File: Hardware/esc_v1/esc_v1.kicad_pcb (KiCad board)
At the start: 6 copper layers, 81 x 51.1 mm, 152 parts, among them IC1 RT8259GE, J1 vcc_connector, J2 SWD_tag_connect, J3 motor_connector, J4 10118193-0001LF, Q1 IRFH7084TRPBF, Q2 IRFH7084TRPBF, Q3 IRFH7084TRPBF, Q4 IRFH7084TRPBF, Q5 IRFH7084TRPBF, Q6 IRFH7084TRPBF, SW1 SW_Push, U1 FAN7390MX, U10 MAX40056UAUA/V+, U2 AZ1117CH-3.3TRG1, U3 FAN7390MX, U4 ATSAME70J21A-AN, U5 CP2102N-Axx-xQFN24, U6 FAN7390MX, U9 MAX40056UAUA/V+, Y1 Crystal_GND2

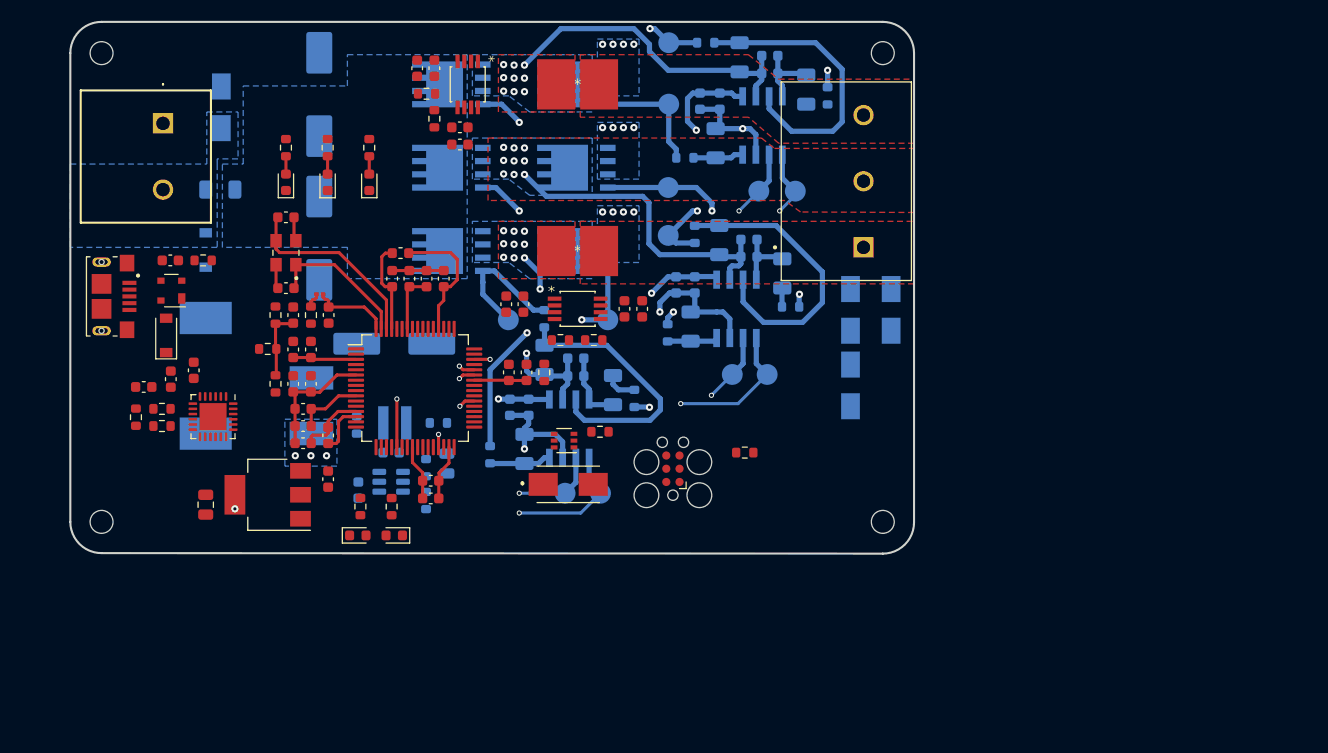
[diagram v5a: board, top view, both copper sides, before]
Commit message: Finished layout. Final check remains
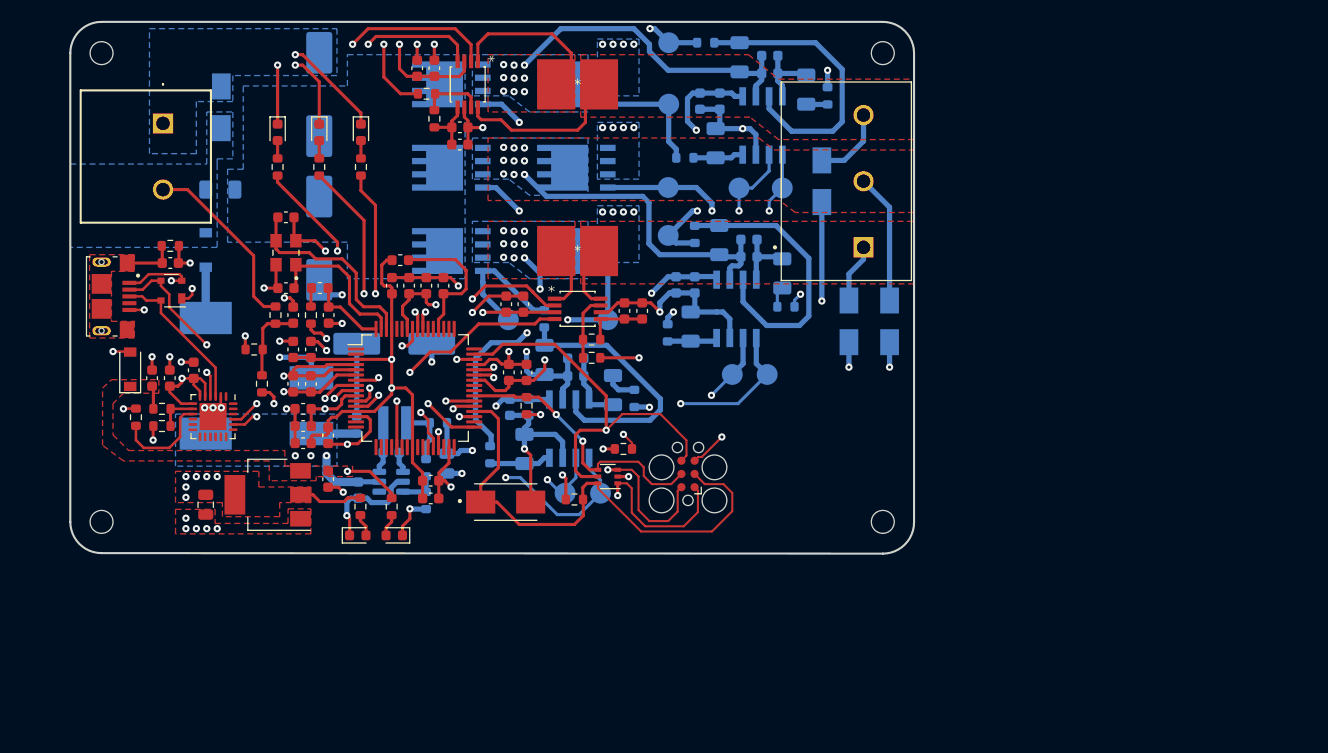
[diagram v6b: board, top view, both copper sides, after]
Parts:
- L2: footprint Inductor_SMD:L_0201_0603Metric -> Inductor_SMD:L_0603_1608Metric
- moved D8 14.0 mm to (163.6, 95.2)
- moved R14 11.7 mm to (144.5, 120.8)
- moved D1 10.0 mm to (111.3, 90.5), turned to -90 degrees
- moved R1 8.99 mm to (111.3, 93.8), turned to 90 degrees
- moved D5 8.65 mm to (119.3, 90.5), turned to -90 degrees
- moved R3 7.44 mm to (119.3, 93.8), turned to 90 degrees
- moved R16 6.95 mm to (139.8, 125.7), turned to 0 degrees
- moved SW1 6.24 mm to (132.8, 126.0)
- moved D6 6.15 mm to (166.2, 108.6)
- moved D2 5.44 mm to (143.0, 123.5)
- moved D4 4.86 mm to (115.3, 90.5), turned to -90 degrees
- moved D23 4.74 mm to (97.2, 113.2)
- moved D7 3.91 mm to (170.1, 108.6)
- moved R15 3.62 mm to (135.2, 116.7), turned to 90 degrees
- moved R33 3.45 mm to (141.4, 112.1), turned to 0 degrees
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- renumbered H0 to TP1, LO_W to TP10, HO_W to TP11, LO_W to TP12, L0 to TP2, H1 to TP3, L1 to TP4, H2 to TP5, L2 to TP6, HO_U to TP7, LO_U to TP8, HO_V to TP9
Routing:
- net GND: track 65.4 -> 208.7 mm, vias 15 -> 65
- net +3V3: track 17.6 -> 95.3 mm, vias 1 -> 19
- net /MCU/overcurr_err_U: track 0.00 -> 54.4 mm, vias 0 -> 2
- net /MCU/curr_sense_U: track 0.00 -> 50.1 mm, vias 0 -> 2
- net /NRST: track 0.00 -> 48.8 mm
- net /TRACESWO: track 0.00 -> 38.9 mm, vias 0 -> 1
- net /SWDIO: track 0.11 -> 33.7 mm, vias 0 -> 3
- net /SWCLK: track 0.00 -> 26.5 mm, vias 0 -> 2
- net /MCU/UART0_TX: track 0.00 -> 26.3 mm, vias 0 -> 2
- net /MCU/LED_0: track 0.00 -> 24.9 mm, vias 0 -> 2
- net /MCU/overcurr_err_V: track 0.00 -> 23.6 mm, vias 0 -> 2
- net /PHASE_U: track 0.00 -> 23.5 mm
- net /MCU/UART0_RX: track 0.00 -> 23.5 mm, vias 0 -> 2
- net /MCU/curr_sense_V: track 0.00 -> 22.8 mm, vias 0 -> 2
- net /MCU/LED_1: track 0.00 -> 20.8 mm, vias 0 -> 2
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- added copper zone on F.Cu, net +3V3
- added copper zone on F.Cu, net +5V
- added copper zone on In2.Cu, net +5V
- added copper zone on F.Cu, net /shield
- added copper zone on F.Cu, net GND

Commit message: Removed USB to serial chip and added serial connector. Finished layout, made production files and sent to production
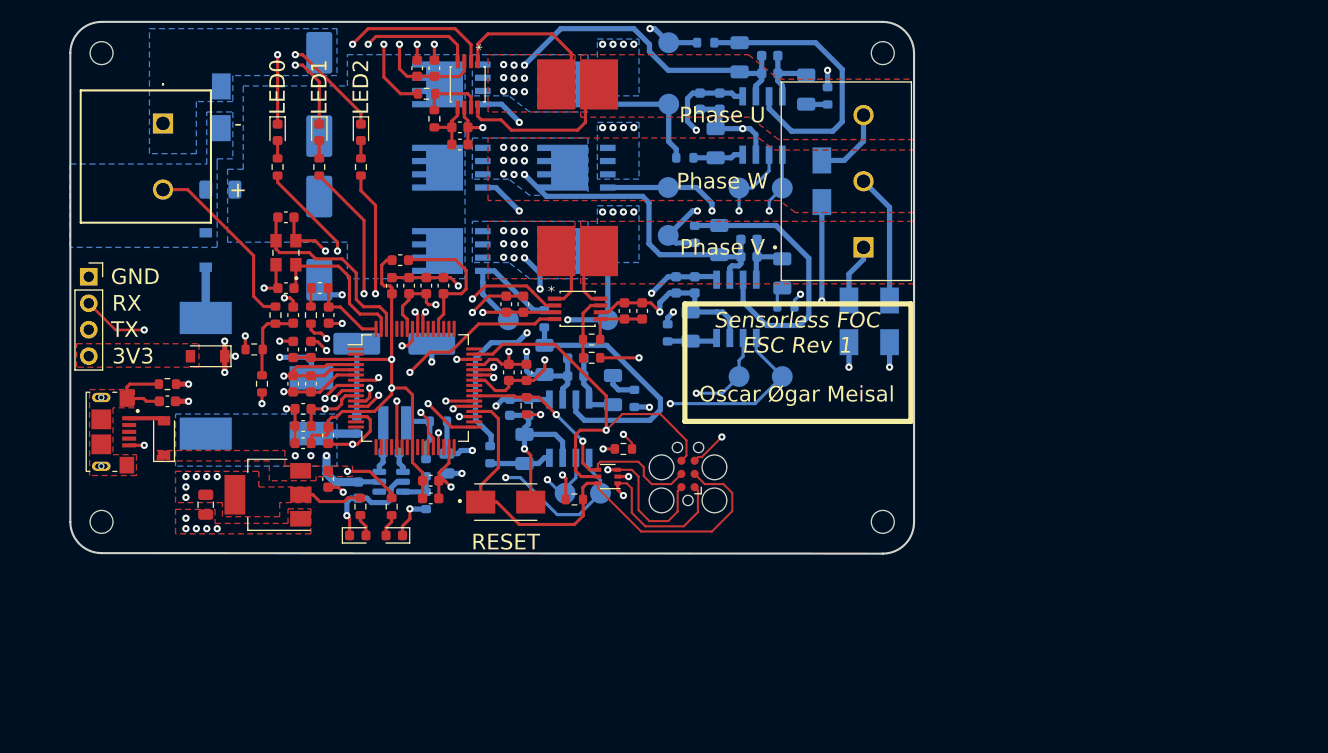
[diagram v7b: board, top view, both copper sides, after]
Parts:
- removed C30: 1uF, Capacitor_SMD:C_0603_1608Metric
- removed C31: 4.7uF, Capacitor_SMD:C_0603_1608Metric
- removed C32: 0.1uF, Capacitor_SMD:C_0603_1608Metric
- removed R17: 22.1K, Resistor_SMD:R_0603_1608Metric
- removed R18: 47.5K, Resistor_SMD:R_0603_1608Metric
- removed R19: 1K, Resistor_SMD:R_0603_1608Metric
- removed U5: CP2102N-Axx-xQFN24, Package_DFN_QFN:QFN-24-1EP_4x4mm_P0.5mm_EP2.6x2.6mm
- added J5: Conn_01x04, Connector_PinSocket_2.54mm:PinSocket_1x04_P2.54mm_Vertical, F.Cu at (93.2, 104.3)
- D9: value SP0503BAHT -> D_Schottky; footprint Package_TO_SOT_SMD:SOT-143 -> Diode_SMD:D_SOD-123
- moved C1 13.3 mm to (100.7, 116.3)
- moved R4 13.3 mm to (100.7, 114.6)
- moved J4 13.0 mm to (94.4, 119.2)
- moved D23 7.36 mm to (100.4, 119.8)
- moved D9 7.19 mm to (104.6, 112.0)
- moved TP5 1.46 mm to (159.8, 113.9)
- moved TP6 0.68 mm to (155.6, 113.9)
- moved R11 0.15 mm to (126.7, 118.2)
- renumbered IC1 to U7
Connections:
- D9 pad 1: GND -> +3V3
- D9 pad 2: /VBUS -> Net-(D9-Pad2)
- J4 pad 2: /USB_DM -> unconnected-(J4-Pad2)
- J4 pad 3: /USB_DP -> unconnected-(J4-Pad3)
- U4 pad 28: /MCU/UART0_RX -> /UART0_RX
- U4 pad 33: /MCU/UART0_TX -> /UART0_TX
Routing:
- net /UART0_TX: track 0.00 -> 43.0 mm, vias 0 -> 1
- net /UART0_RX: track 0.00 -> 41.5 mm, vias 0 -> 2
- net /MCU/UART0_TX: track 26.3 -> 0.00 mm, vias 2 -> 0
- net /MCU/UART0_RX: track 23.5 -> 0.00 mm, vias 2 -> 0
- net /USB_DM: track 16.5 -> 0.00 mm, vias 2 -> 0
- net /VBUS: track 18.4 -> 3.53 mm, vias 2 -> 0
- net /USB_DP: track 14.6 -> 0.00 mm
- net Net-(R19-Pad2): track 9.58 -> 0.00 mm
- net +3V3: track 95.3 -> 87.7 mm, vias 19 -> 20
- net GND: track 208.7 -> 201.4 mm, vias 65 -> 58
- net /UART_USB_BRIDGE/VBUS: track 3.79 -> 0.00 mm
- net /shield: track 5.05 -> 7.52 mm
- net +5V: track 13.3 -> 11.1 mm
- net /MCU/PWM_H2: track 38.9 -> 41.1 mm
- net /MCU/PWM_L2: track 43.9 -> 44.5 mm
- added copper zone on F.Cu, net Net-(D9-Pad2)
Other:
- board text added: "+"
- board text added: "-"
- board text added: "3V3"
- board text added: "GND"
- board text added: "LED0"
- board text added: "LED1"
- board text added: "LED2"
- board text added: "Oscar Øgar Meisal"
- board text added: "Phase U"
- board text added: "Phase V"
- board text added: "Phase W"
- board text added: "RESET"
- board text added: "RX"
- board text added: "Sensorless FOC ESC Rev 1"
- board text added: "TX"
